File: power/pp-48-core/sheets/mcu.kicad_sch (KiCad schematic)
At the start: 19 parts, among them J5 SWD, U3 STM32G070CBT6, Y1 8MHz

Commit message: pp-48 plane boards: press deadline line (docs/press-deadline-line.md decided: option B + A) on a 14-pin chain (S14B-PH-K-S C157938; 13 PRESS_EN, 14 EXP_RSTN, cable n -> 15 - n, pins v 35..61); unit Q10 / R31 switch the photoMOS LED returns (PRESS_RTN), core U301 74LVC1G123 deadline (pp:74LVC1G123 single-unit copy) on PC6 PRESS_TRIG, PC7 EXP_RSTN to the units' /RESET; ERC 0 both; boards rebuilt and placed, unit 78.5 x 72 with the strip power path re-placed top-down; unit routing tools (route_unit.py hand copper + In2 band / +3V3 trunk, unitsplit.py, route_unit.sh flow): DRC 0 errors, ~10 unconnected at expander U5; core placed, not routed; pmmount.py restored from granite_controller; ADR 0005 decision 4; handoff
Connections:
- net PRESS_TRIG: now reaches U3.30 (PC6)
- net EXP_RSTN: now reaches U3.31 (PC7)
- no-connect marks 29 -> 27
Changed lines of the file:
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@@
-	)
-	(no_connect
-		(at 185.42 157.48)
-	)
-	(no_connect
-		(at 185.42 160.02)
 	)
 	(no_connect
@@
 		(effects
 			(font
+				(size 1.27 1.27)
+			)
+			(justify right)
+		)
+	)
+	(hierarchical_label "PRESS_TRIG"
+		(shape output)
+		(at 185.42 157.48 180)
+		(effects
+			(font
+				(size 1.27 1.27)
+			)
+			(justify right)
+		)
+	)
+	(hierarchical_label "EXP_RSTN"
+		(shape output)
+		(at 185.42 160.02 180)
+		(effects
+			(font

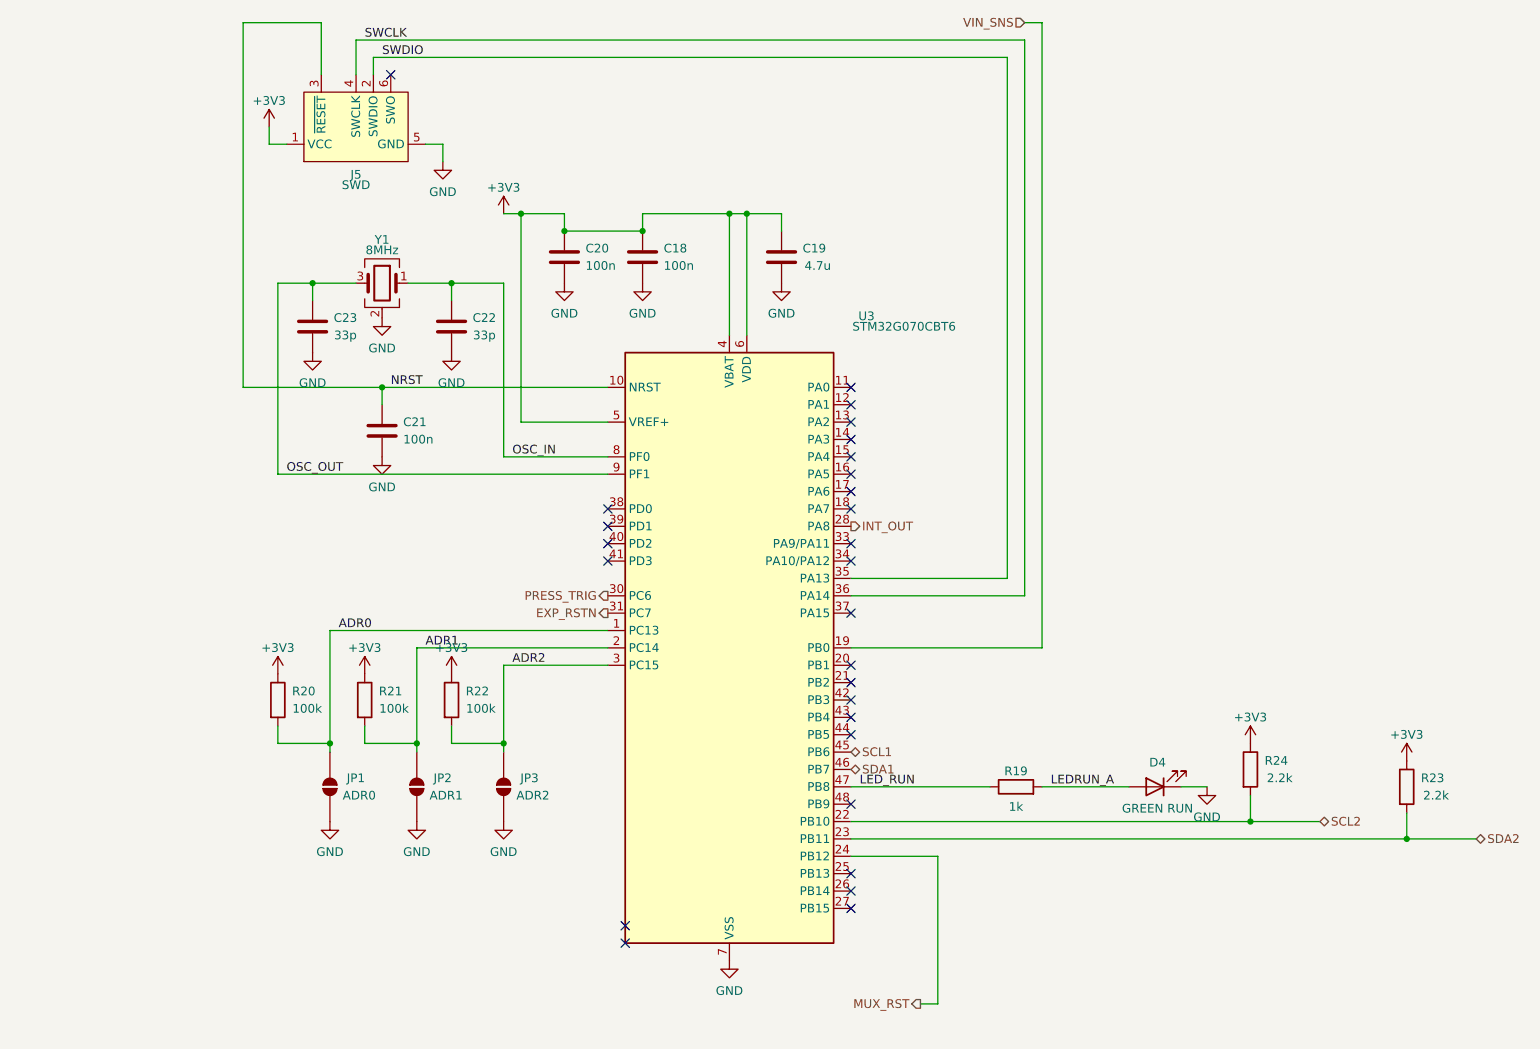
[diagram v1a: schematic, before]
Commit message: pp-48 core MCU: pins reassigned for the fewest ratsnest crossings on the core board (38 -> 13): I2C1 PB8 / PB9, I2C2 PA11 / PA12, VIN_SNS PB11, PRESS_TRIG PB12, MUX_RST PB13, LED_RUN PB14, EXP_RSTN PD0, INT_OUT PD2, ADR0-2 PA15 / PD1 / PA8; MCU sheet drawn from the pin map (ports / labels at the pins); gensch.py core writes firmware/plane-core-pins.toml from the same table; ADR 0002 pin table, ADR 0005 and the press-deadline note follow; ERC 0
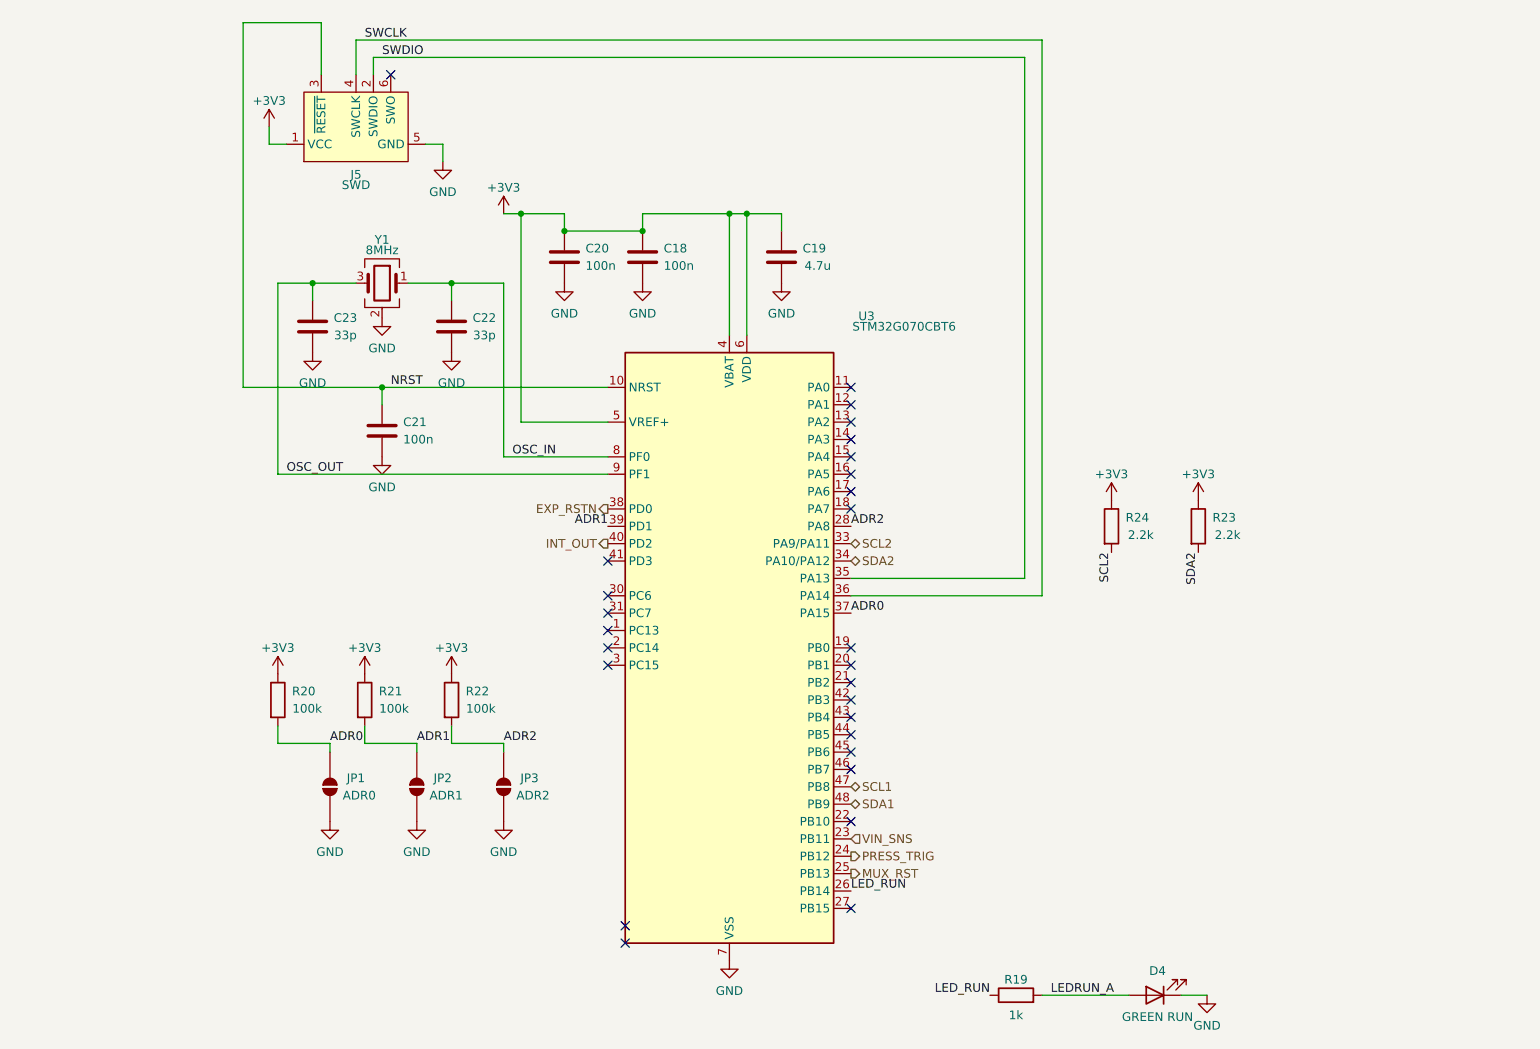
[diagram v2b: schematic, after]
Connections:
- net ADR0: now also U3.37 (PA15); no longer U3.1 (PC13)
- net ADR1: now also U3.39 (PD1); no longer U3.2 (PC14)
- net ADR2: now also U3.28 (PA8); no longer U3.3 (PC15)
- net EXP_RSTN: now also U3.38 (PD0); no longer U3.31 (PC7)
- net INT_OUT: now also U3.40 (PD2); no longer U3.28 (PA8)
- net LED_RUN: now also U3.26 (PB14); no longer U3.47 (PB8)
- net MUX_RST: now also U3.25 (PB13); no longer U3.24 (PB12)
- net PRESS_TRIG: now also U3.24 (PB12); no longer U3.30 (PC6)
- net SCL1: now also U3.47 (PB8); no longer U3.45 (PB6)
- net SCL2: now also U3.33 (PA9/PA11); no longer U3.22 (PB10)
- net SDA1: now also U3.48 (PB9); no longer U3.46 (PB7)
- net SDA2: now also U3.34 (PA10/PA12); no longer U3.23 (PB11)
- net VIN_SNS: now also U3.23 (PB11); no longer U3.19 (PB0)
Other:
- moved on the sheet: D4, R19, R23, R24

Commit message: pp-48-core: GND stitch (1 via), silk (23 refs placed, 71 small ones hidden), JLC outputs; LCSC codes for the 25 passive values that had none (sch/draw.py BASIC table, JLC parts API: basic where JLC has one), copied onto the routed board; BOM 86 parts, left out only CV1/CV2, holes, J5 / JP1-3 (copper only) and DNP R28 / R29; DRC 0 unconnected, parity clean, isocheck clean
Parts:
- C19: LCSC (none) -> C19666
- C22, C23: LCSC (none) -> C1562
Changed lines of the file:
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@@
 			)
 		)
-		(property "LCSC" ""
+		(property "LCSC" "C19666"
 			(at 210.82 107.95 0)
 			(hide yes)
@@
 			)
 		)
-		(property "LCSC" ""
+		(property "LCSC" "C1562"
 			(at 162.56 118.11 0)
 			(hide yes)
@@
 			)
 		)
-		(property "LCSC" ""
-			(at 142.24 118.11 0)
-			(hide yes)
+		(property "LCSC" "C1562"
+			(at 142.24 118.11 0)
+			(hide yes)

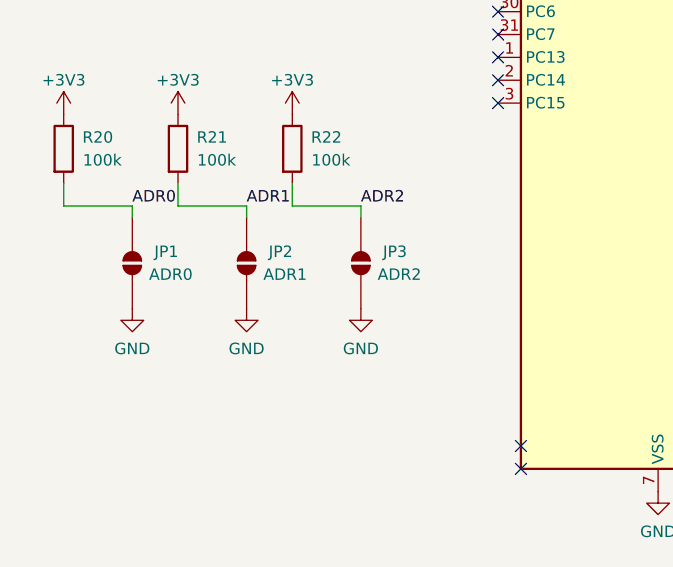
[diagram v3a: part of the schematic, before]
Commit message: pp-48-core address straps: solder jumpers JP1-3 -> 3-way SMD DIP switch SW1 (KingTek DSHP03TSGET, C50844, 1.27 mm pitch, KiCad footprint and model) on F right of U3, ON = 0, plane address 0x30 + ADR[2:0]; swapped on the routed board (ADR0-2, +3V3 and SWDIO rerouted with krt-reroute --keep, one mazefix GND hop, mergetracks, silk, fill), core.py table updated for a rebuild; ERC 0, DRC 0 unconnected, parity clean, isocheck clean, BOM 87 parts; handoff
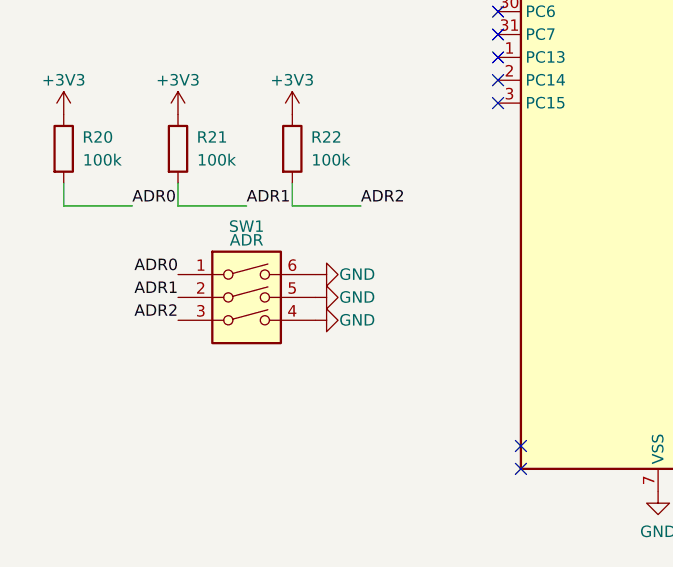
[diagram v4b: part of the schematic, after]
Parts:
- removed JP1: ADR0, Jumper:SolderJumper-2_P1.3mm_Open_RoundedPad1.0x1.5mm, symbol Jumper:SolderJumper_2_Open
- removed JP2: ADR1, Jumper:SolderJumper-2_P1.3mm_Open_RoundedPad1.0x1.5mm, symbol Jumper:SolderJumper_2_Open
- removed JP3: ADR2, Jumper:SolderJumper-2_P1.3mm_Open_RoundedPad1.0x1.5mm, symbol Jumper:SolderJumper_2_Open
- added SW1: ADR, Button_Switch_SMD:SW_DIP_SPSTx03_Slide_KingTek_DSHP03TS_W7.62mm_P1.27mm, symbol Switch:SW_DIP_x03
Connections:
- net ADR0: now also SW1.1
- net ADR1: now also SW1.2
- net ADR2: now also SW1.3
- net GND: now also SW1.4, SW1.5, SW1.6

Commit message: pp-48-core SWD: J6 ARM Cortex 10-pin header (Samtec FTSH-105-01-L-DV-K, C5155080, keyed shroud) on F right of U3 below SW1, for stock probe ribbons; the Tag-Connect pads J5 stay; J6 drawn as Conn_02x05 (two ARM SWD symbols on one net are output-to-output in ERC); SWDIO / SWCLK / NRST / +3V3 routed with krt-reroute --keep, silk, fill; ERC 0, DRC 0 unconnected, parity clean, isocheck clean, BOM 88 parts; handoff
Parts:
- added J6: SWD, Connector_PinHeader_1.27mm:PinHeader_2x05_P1.27mm_Vertical_SMD, symbol Connector_Generic:Conn_02x05_Odd_Even
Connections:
- net +3V3: now also J6.1 (Pin_1)
- net GND: now also J6.3 (Pin_3), J6.5 (Pin_5), J6.9 (Pin_9)
- net NRST: now also J6.10 (Pin_10)
- net SWCLK: now also J6.4 (Pin_4)
- net SWDIO: now also J6.2 (Pin_2)
- no-connect marks 27 -> 30
